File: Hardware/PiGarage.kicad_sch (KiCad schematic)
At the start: 76 parts, among them J1 Conn_02x03_Odd_Even, J2 Conn_02x02_Counter_Clockwise, J3 PJ-320B, J4 Conn_02x20_Odd_Even, Q1 AO4407A, Q2 MMBT3904, U1 TPS54560BQDDARQ1, U2 TL431DBZ, U3 PCM5122PWR, U4 AP2112K-3.3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

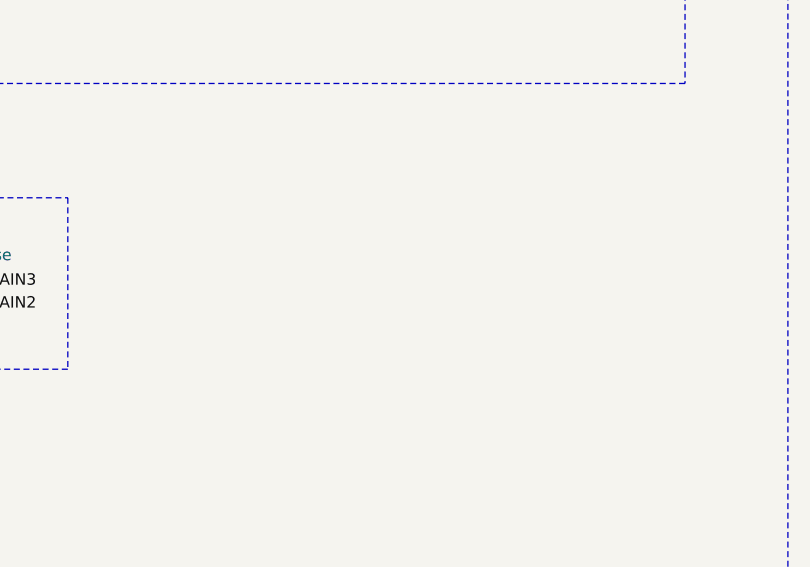
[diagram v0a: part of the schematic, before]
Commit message: Add J5 JST SH 1.0mm fan output connector
Adds a 2-pin JST SH 1.0mm (BM02B-SRSS-TB) fan power header to the schematic.
Pin 1 = +5V, Pin 2 = GND. Taps the unfiltered 5V rail near U1 (buck converter)
for a 25mm cooling fan. Same connector family as the RPi 5 fan.

Updated docs: README features list, BOM/design-notes.txt (new J5 section,
hand-solder list), and Docs/ordering-guide.md (hand-solder step).
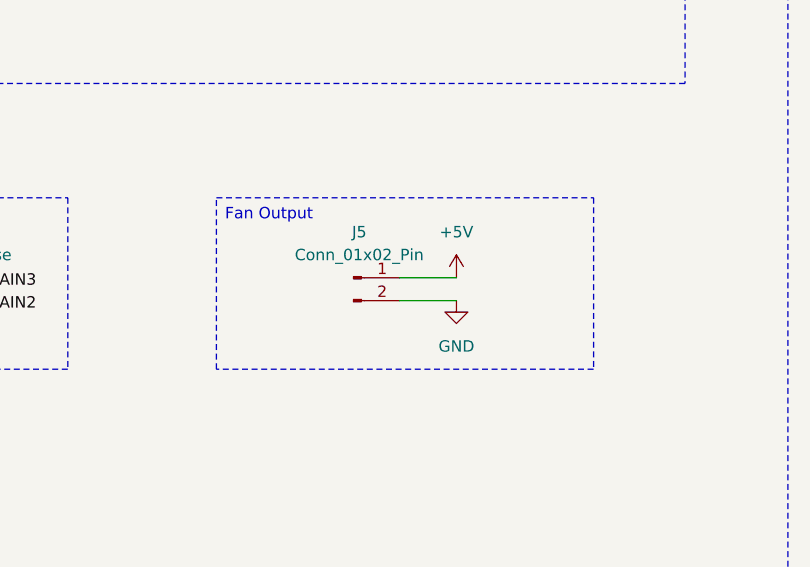
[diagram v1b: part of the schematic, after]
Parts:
- added J5: Conn_01x02_Pin, Connector_JST:JST_SH_BM02B-SRSS-TB_1x02-1MP_P1.00mm_Vertical, symbol Connector:Conn_01x02_Pin
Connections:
- net +5V: now also J5.1 (Pin_1)
- net GND: now also J5.2 (Pin_2)

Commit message: Swap J5 fan connector: JST SH 1.0mm SMD → JST PH 2.0mm through-hole
B2B-PH-K-S (C131337) replaces BM02B-SRSS-TB. Through-hole, keyed,
locking tab — better suited to automotive vibration. Relocated J5
near U1/L1 so fan sits directly over the buck converter hotspot.
Mating: PHR-2 housing + SPH-002T-P0.5L contacts.

Updated schematic footprint, PCB layout, BOM design-notes, and
ordering guide. Notes that C131337 is Extended (~$3 fee) so
hand-soldering is recommended over JLCPCB assembly for this part.
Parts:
- J5: footprint Connector_JST:JST_SH_BM02B-SRSS-TB_1x02-1MP_P1.00mm_Vertical -> Connector_JST:JST_PH_B2B-PH-K_1x02_P2.00mm_Vertical
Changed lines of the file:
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@@
 			)
 		)
-		(property "Footprint" "Connector_JST:JST_SH_BM02B-SRSS-TB_1x02-1MP_P1.00mm_Vertical"
+		(property "Footprint" "Connector_JST:JST_PH_B2B-PH-K_1x02_P2.00mm_Vertical"
 			(at 184.15 111.76 0)
 			(hide yes)
